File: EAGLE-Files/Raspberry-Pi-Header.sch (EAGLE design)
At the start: 3 parts

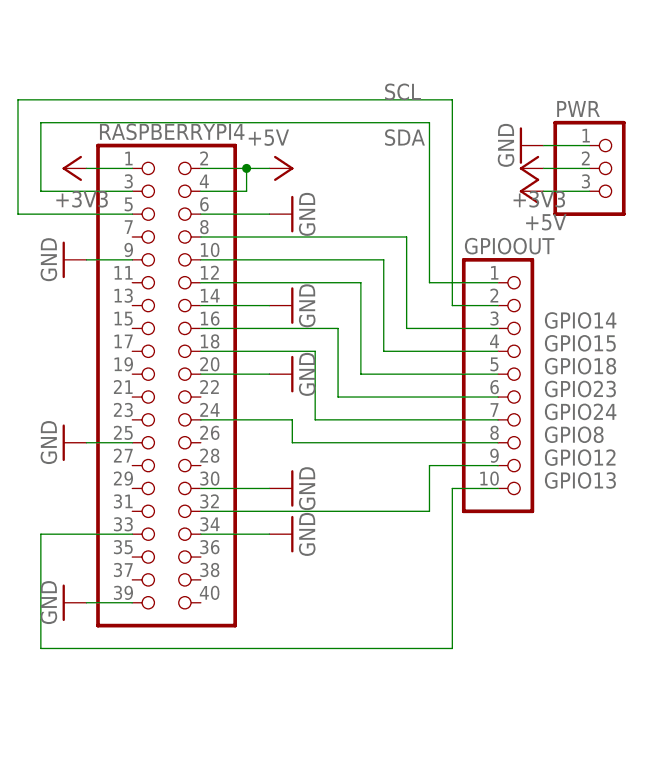
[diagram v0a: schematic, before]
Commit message: * Updated the header board * Added a audio board * Added a power controller board * Updated gitignore
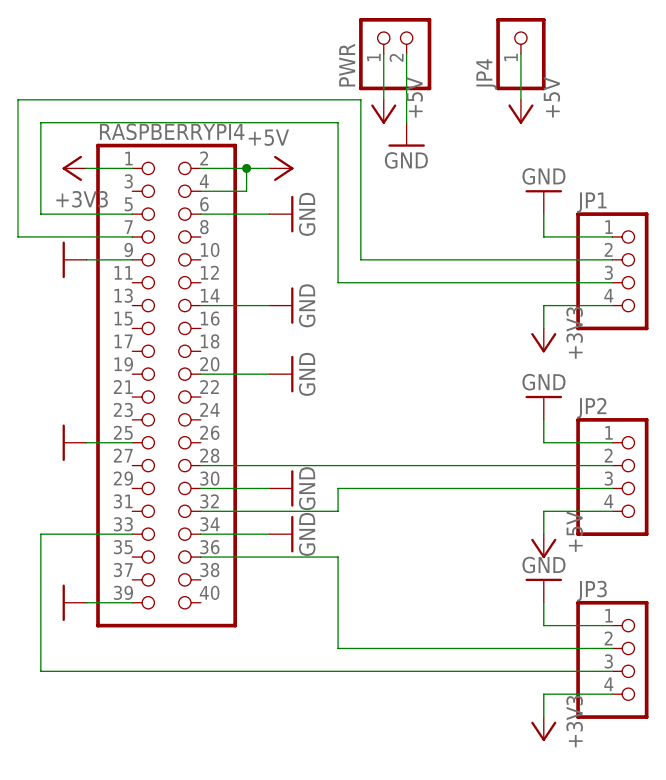
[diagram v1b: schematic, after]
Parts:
- removed GPIOOUT: (no value), pinhead:PINHD-1X10/90
- added JP1, JP2, JP3: (no value), pinhead:PINHD-1X4/90
- added JP4: (no value), pinhead:PINHD-1X1
- PWR: device pinhead:PINHD-1X3 -> pinhead:PINHD-1X2/90
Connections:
- removed net GPIO14: GPIOOUT.3, RASPBERRYPI4.8
- removed net GPIO15: GPIOOUT.4, RASPBERRYPI4.10
- removed net GPIO18: GPIOOUT.5, RASPBERRYPI4.12
- removed net GPIO23: GPIOOUT.6, RASPBERRYPI4.16
- removed net GPIO24: GPIOOUT.7, RASPBERRYPI4.18
- removed net GPIO8: GPIOOUT.8, RASPBERRYPI4.24
- new net GPIO1: JP2.2, RASPBERRYPI4.28
- new net GPIO16: JP3.2, RASPBERRYPI4.36
- net +3V3: now also JP1.4, JP3.4; no longer PWR.2
- net +5V: now also JP2.4, JP4.1, PWR.1; no longer PWR.3
- net GND: now also JP1.1, JP2.1, JP3.1, PWR.2; no longer PWR.1
- net GPIO12: now also JP2.3; no longer GPIOOUT.9
- net GPIO13: now also JP3.3; no longer GPIOOUT.10
- net SCL: now also JP1.2, RASPBERRYPI4.7; no longer GPIOOUT.2, RASPBERRYPI4.5
- net SDA: now also JP1.3, RASPBERRYPI4.5; no longer GPIOOUT.1, RASPBERRYPI4.3

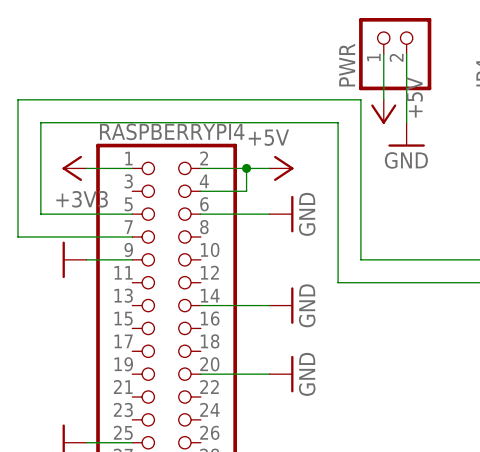
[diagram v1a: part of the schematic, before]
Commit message: * Fixed a small error in the Raspberry Pi GPIO Header board (pins was offset) * Added the initial 3d print files
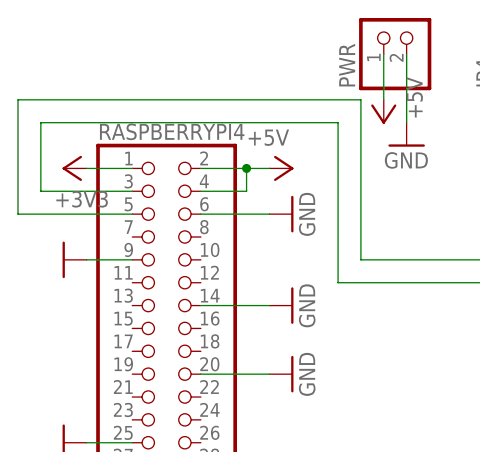
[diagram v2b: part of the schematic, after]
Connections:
- net SCL: now also RASPBERRYPI4.5; no longer RASPBERRYPI4.7
- net SDA: now also RASPBERRYPI4.3; no longer RASPBERRYPI4.5
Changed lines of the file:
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@@
 <wire x1="71.12" y1="60.96" x2="71.12" y2="78.74" width="0.1524" layer="91"/>
 <wire x1="71.12" y1="78.74" x2="33.02" y2="78.74" width="0.1524" layer="91"/>
-<wire x1="33.02" y1="78.74" x2="33.02" y2="63.5" width="0.1524" layer="91"/>
-<pinref part="RASPBERRYPI4" gate="A" pin="7"/>
-<wire x1="33.02" y1="63.5" x2="45.72" y2="63.5" width="0.1524" layer="91"/>
+<pinref part="RASPBERRYPI4" gate="A" pin="5"/>
+<wire x1="45.72" y1="66.04" x2="33.02" y2="66.04" width="0.1524" layer="91"/>
+<wire x1="33.02" y1="66.04" x2="33.02" y2="78.74" width="0.1524" layer="91"/>
 </segment>
 </net>
 <net name="SDA" class="0">
 <segment>
-<pinref part="RASPBERRYPI4" gate="A" pin="5"/>
-<wire x1="45.72" y1="66.04" x2="35.56" y2="66.04" width="0.1524" layer="91"/>
-<wire x1="35.56" y1="66.04" x2="35.56" y2="76.2" width="0.1524" layer="91"/>
 <wire x1="35.56" y1="76.2" x2="68.58" y2="76.2" width="0.1524" layer="91"/>
 <wire x1="68.58" y1="76.2" x2="68.58" y2="58.42" width="0.1524" layer="91"/>
 <pinref part="JP1" gate="A" pin="3"/>
 <wire x1="68.58" y1="58.42" x2="99.06" y2="58.42" width="0.1524" layer="91"/>
+<pinref part="RASPBERRYPI4" gate="A" pin="3"/>
+<wire x1="45.72" y1="68.58" x2="35.56" y2="68.58" width="0.1524" layer="91"/>
+<wire x1="35.56" y1="68.58" x2="35.56" y2="76.2" width="0.1524" layer="91"/>
 </segment>
 </net>
